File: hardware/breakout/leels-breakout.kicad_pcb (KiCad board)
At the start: 2 copper layers, 0 parts

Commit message: Breakout PCB: placement, routing and DRC-clean board
- build_pcb.py builds the board from the schematic netlist: outline (stops
  at the DevKit's PCB edge, nothing under the antenna), placement with
  the buffer and passives under the DevKit, terminals facing the edges,
  GND pours on both layers and stitching vias.
- route.py round-trips through Freerouting (Specctra DSN/SES); GND is
  left to the pours.
- leels.pretty: Espressif's DevKitC-1 footprint with the courtyard
  limited to the socket rows.
- Q1 on TO-92_Inline_Wide (the narrow one breaks 0.25 mm clearance).
- Net classes: 0.3 mm signals, 0.6 mm power and ground.
DRC: 0 violations, 0 unconnected, 0 schematic parity issues.

Co-Authored-By: Claude Opus 5.5 <noreply@anthropic.com>
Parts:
- added C1: 100n, Capacitor_THT:C_Disc_D5.0mm_W2.5mm_P5.00mm, F.Cu at (19.5, 45.2)
- added C2: 10u 16V, Capacitor_THT:CP_Radial_D5.0mm_P2.00mm, F.Cu at (29.5, 45.9)
- added D1: 1N5817, Diode_THT:D_DO-41_SOD81_P10.16mm_Horizontal, F.Cu at (25.0, 69.0)
- added J2: Servo, TerminalBlock_Phoenix:TerminalBlock_Phoenix_MKDS-1,5-5-5.08_1x05_P5.08mm_Horizontal, F.Cu at (45.5, 35.0)
- added J3: Encoder, TerminalBlock_Phoenix:TerminalBlock_Phoenix_MKDS-1,5-5-5.08_1x05_P5.08mm_Horizontal, F.Cu at (5.50, 43.0)
- added J4: 5V in, TerminalBlock_Phoenix:TerminalBlock_Phoenix_MKDS-1,5-2-5.08_1x02_P5.08mm_Horizontal, F.Cu at (45.5, 62.0)
- added J5: Nextion, Connector_JST:JST_XH_B4B-XH-A_1x04_P2.50mm_Vertical, F.Cu at (46.0, 27.7)
- added J6: Shield GND, TerminalBlock_Phoenix:TerminalBlock_Phoenix_MKDS-1,5-3-5.08_1x03_P5.08mm_Horizontal, F.Cu at (5.50, 61.2)
- added Q1: 2N3904, Package_TO_SOT_THT:TO-92_Inline_Wide, F.Cu at (24.1, 13.0)
- added R1: 1k, Resistor_THT:R_Axial_DIN0207_L6.3mm_D2.5mm_P7.62mm_Horizontal, F.Cu at (33.0, 17.0)
- added R2: 10k, Resistor_THT:R_Axial_DIN0207_L6.3mm_D2.5mm_P7.62mm_Horizontal, F.Cu at (25.4, 20.5)
- added R3: 4k7, Resistor_THT:R_Axial_DIN0207_L6.3mm_D2.5mm_P7.62mm_Horizontal, F.Cu at (16.8, 52.0)
- added R4: 4k7, Resistor_THT:R_Axial_DIN0207_L6.3mm_D2.5mm_P7.62mm_Horizontal, F.Cu at (16.8, 55.5)
- added R5: 10k, Resistor_THT:R_Axial_DIN0207_L6.3mm_D2.5mm_P7.62mm_Horizontal, F.Cu at (27.0, 52.0)
- added R6: 10k, Resistor_THT:R_Axial_DIN0207_L6.3mm_D2.5mm_P7.62mm_Horizontal, F.Cu at (27.0, 55.5)
- added R7: 4k7, Resistor_THT:R_Axial_DIN0207_L6.3mm_D2.5mm_P7.62mm_Horizontal, F.Cu at (16.8, 59.0)
- added U1: ESP32-C6-DevKitC-1, leels:ESP32-C6-DevKitC-1_Sockets, F.Cu at (14.0, 10.0)
- added U2: 74AHCT125, Package_DIP:DIP-14_W7.62mm, F.Cu at (32.0, 40.5)
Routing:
- net +5V: track 0.00 -> 96.5 mm
- net ENC_Z: track 0.00 -> 73.7 mm
- net +3V3: track 0.00 -> 72.4 mm
- net Net-(J2-Pin_4): track 0.00 -> 44.6 mm
- net Net-(J3-Pin_4): track 0.00 -> 38.0 mm
- net Net-(U1-GPIO19): track 0.00 -> 33.0 mm
- net Net-(J3-Pin_3): track 0.00 -> 32.7 mm
- net Net-(J2-Pin_3): track 0.00 -> 26.4 mm
- net Net-(U1-GPIO18): track 0.00 -> 24.0 mm
- net Net-(J2-Pin_2): track 0.00 -> 15.4 mm
- net Net-(D1-A): track 0.00 -> 13.2 mm
- net Net-(U1-GPIO20): track 0.00 -> 13.1 mm
- net Net-(J5-Pin_3): track 0.00 -> 9.16 mm
- net Net-(J5-Pin_4): track 0.00 -> 9.14 mm
- net Net-(Q1-B): track 0.00 -> 8.02 mm
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- added copper zone on B.Cu, net GND
- added copper zone on F.Cu, net GND
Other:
- board outline added: 51 x 63.6 mm
- rule pad_to_mask_clearance: 0.05 -> 0

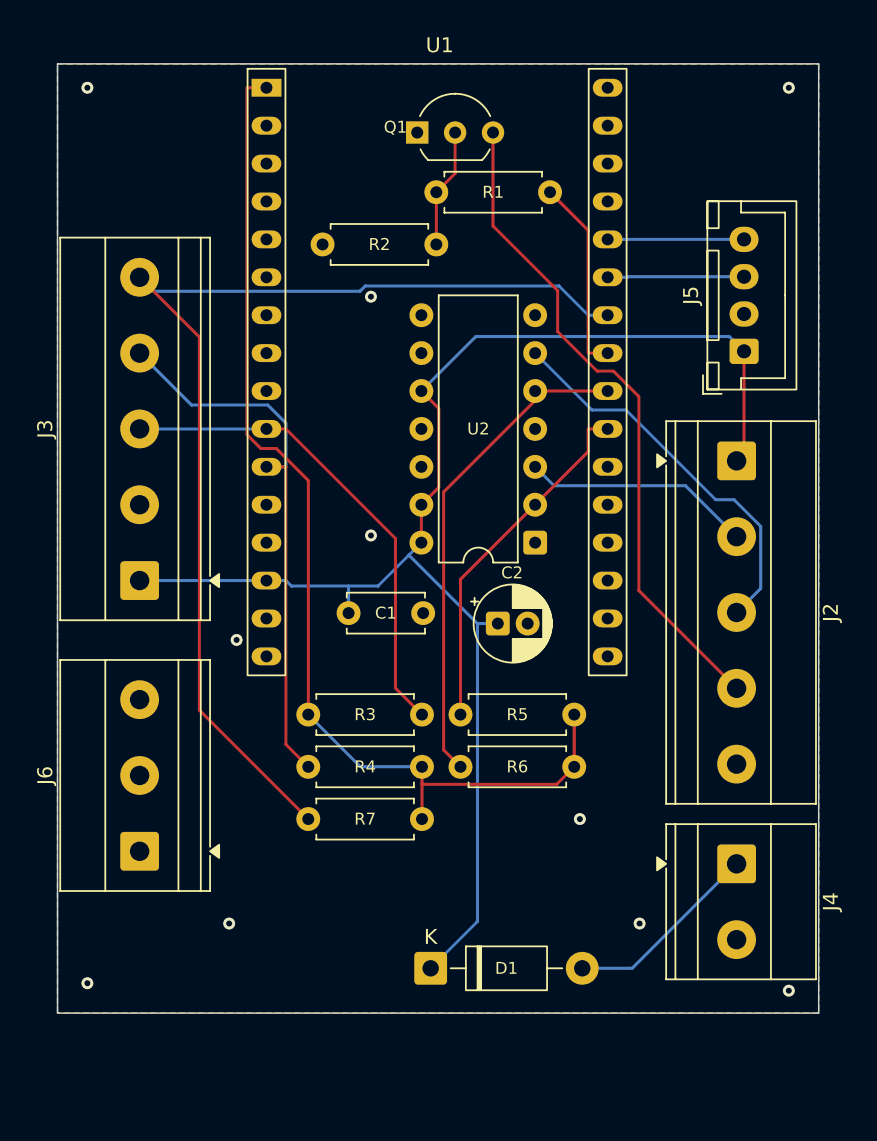
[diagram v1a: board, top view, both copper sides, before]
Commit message: Breakout PCB: caps out from under the DevKit, connector silkscreen
- C1/C2 move below the DevKit (too tall for the ~7 mm under it), next to
  the 5 V input.
- Pin labels beside every terminal and the Nextion header (the display's
  pin names), group titles, board name and orientation on the back.
- Re-routed; DRC 0 violations, 0 unconnected, 0 parity issues.

Co-Authored-By: Claude Opus 5.5 <noreply@anthropic.com>
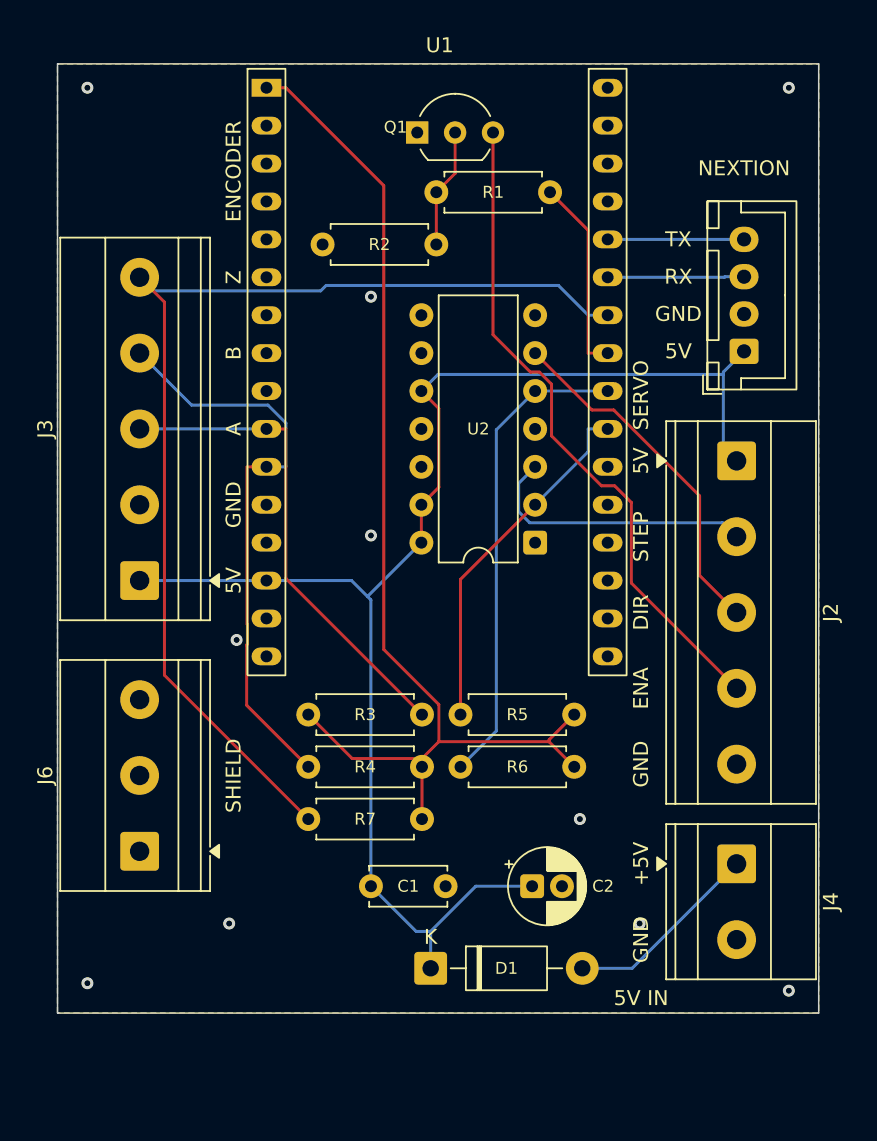
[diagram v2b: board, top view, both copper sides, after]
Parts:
- moved C1 18.4 mm to (21.0, 63.5)
- moved C2 17.7 mm to (31.8, 63.5)
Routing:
- net +3V3: track 72.4 -> 76.1 mm
- net Net-(J2-Pin_2): track 15.4 -> 18.8 mm
- net Net-(J2-Pin_3): track 26.4 -> 23.8 mm
- net Net-(J3-Pin_4): track 38.0 -> 39.1 mm
- net Net-(U1-GPIO19): track 33.0 -> 32.1 mm
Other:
- board text added: "+5V"
- board text added: "5V"
- board text added: "5V IN"
- board text added: "A"
- board text added: "B"
- board text added: "DIR"
- board text added: "DevKitC-1 on top, USB down"
- board text added: "ENA"
- board text added: "ENCODER"
- board text added: "GND"
- board text added: "NEXTION"
- board text added: "RX"
- board text added: "SERVO"
- board text added: "SHIELD"
- board text added: "STEP"
- board text added: "TX"
- board text added: "Z"
- board text added: "leels breakout rev A"

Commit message: Breakout PCB review fixes: terminals face out, real track widths
- Every screw terminal opened towards the DevKit (checked in a 3D
  render); turned all four 180 degrees so wires enter from the edges.
- The routed board was 0.2 mm everywhere: standalone pcbnew doesn't put
  the project's net classes into the DSN. route.py now writes the DSN net
  classes itself: 0.6 mm power, 0.3 mm signals, 0.25 mm clearance.
- Connector references to F.Fab (titles name them), two more stitching
  vias, 3D render added.
DRC: 1 warning (J5 GND thermal on B.Cu, connected via F.Cu), 0
unconnected, 0 parity issues.

Co-Authored-By: Claude Opus 5.5 <noreply@anthropic.com>
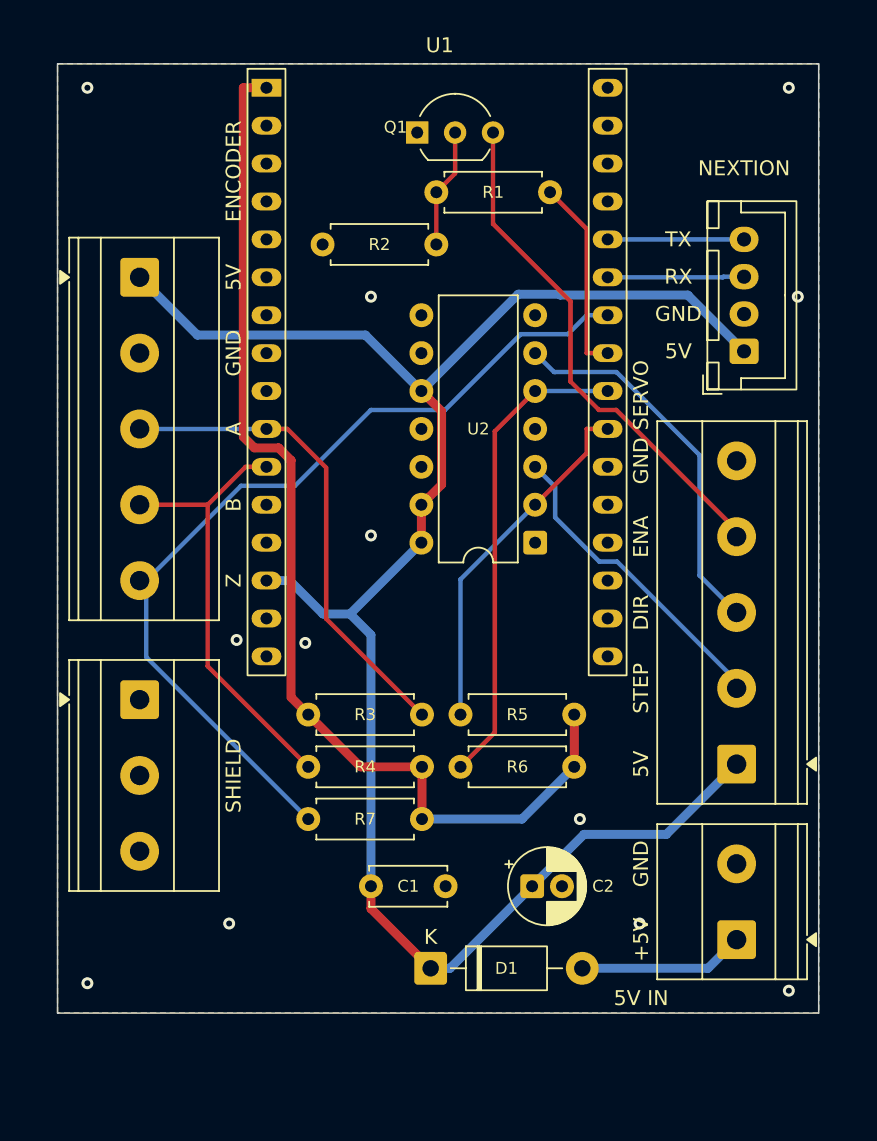
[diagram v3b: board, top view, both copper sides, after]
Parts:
- moved J3 20.3 mm to (5.50, 22.7), turned to -90 degrees
- moved J2 20.3 mm to (45.5, 55.3), turned to 90 degrees
- moved J6 10.2 mm to (5.50, 51.0), turned to -90 degrees
- moved J4 5.08 mm to (45.5, 67.1), turned to 90 degrees
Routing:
- net +5V: track 96.2 -> 124.6 mm
- net ENC_Z: track 73.7 -> 59.2 mm
- net Net-(J2-Pin_4): track 44.9 -> 34.5 mm
- net Net-(J3-Pin_4): track 39.1 -> 29.9 mm
- net Net-(J2-Pin_2): track 18.8 -> 21.1 mm
- net +3V3: track 76.1 -> 74.0 mm
- net Net-(D1-A): track 13.2 -> 11.1 mm
- net Net-(J2-Pin_3): track 23.8 -> 25.4 mm
- net GND: vias 10 -> 12

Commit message: Breakout rev A: encoder RC filters, Nextion before D1, Dupont header, holes
- Encoder A/B/Z: 220R series at the terminal, 220p to GND at the GPIO
  (with the existing 4k7 pull-up), for noise and ESD.
- Nextion power (J5, new J7) on 5V_IN ahead of D1: no Schottky drop for
  the display; it needs J4 power.
- J7: 1x4 2.54 mm header in parallel with the JST for Dupont plugs.
- C1 axial (laid flat) right at U2's supply pin; Q1 laid flat
  (TO-92 staggered horizontal, clearance-safe).
- Three M3 mounting holes; board 51 x 70.1 mm.
DRC: 1 warning (U2 pin 12 thermal on F.Cu, connected via B.Cu), 0
unconnected, 0 parity issues; ERC clean.

Co-Authored-By: Claude Opus 5.5 <noreply@anthropic.com>
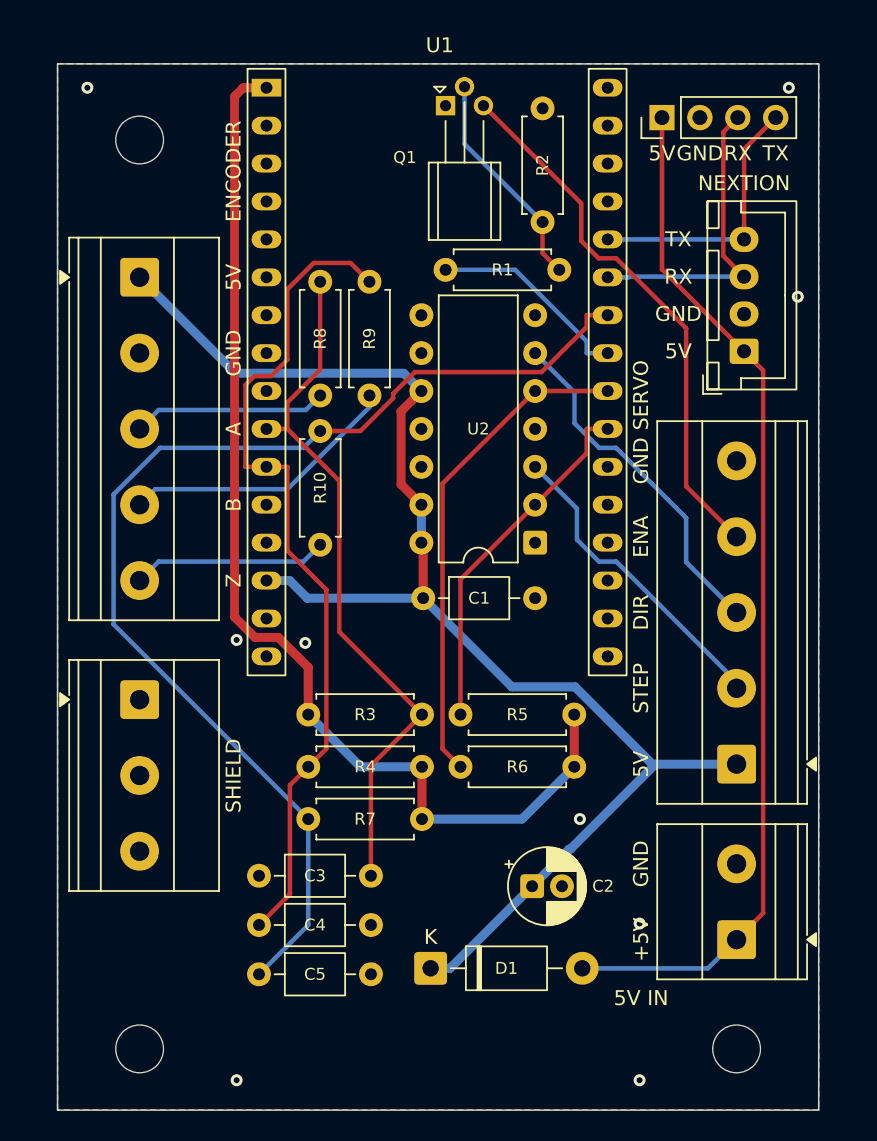
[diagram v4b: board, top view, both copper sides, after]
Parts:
- added C3: 220p, Capacitor_THT:C_Axial_L3.8mm_D2.6mm_P7.50mm_Horizontal, F.Cu at (13.5, 62.8)
- added C4: 220p, Capacitor_THT:C_Axial_L3.8mm_D2.6mm_P7.50mm_Horizontal, F.Cu at (13.5, 66.1)
- added C5: 220p, Capacitor_THT:C_Axial_L3.8mm_D2.6mm_P7.50mm_Horizontal, F.Cu at (13.5, 69.4)
- added H1: MountingHole_3.2mm_M3, MountingHole:MountingHole_3.2mm_M3, F.Cu at (5.50, 13.5)
- added H2: MountingHole_3.2mm_M3, MountingHole:MountingHole_3.2mm_M3, F.Cu at (5.50, 74.4)
- added H3: MountingHole_3.2mm_M3, MountingHole:MountingHole_3.2mm_M3, F.Cu at (45.5, 74.4)
- added J7: Nextion (Dupont), Connector_PinHeader_2.54mm:PinHeader_1x04_P2.54mm_Vertical, F.Cu at (40.5, 12.0)
- added R10: 220, Resistor_THT:R_Axial_DIN0207_L6.3mm_D2.5mm_P7.62mm_Horizontal, F.Cu at (17.6, 40.6)
- added R8: 220, Resistor_THT:R_Axial_DIN0207_L6.3mm_D2.5mm_P7.62mm_Horizontal, F.Cu at (17.6, 30.6)
- added R9: 220, Resistor_THT:R_Axial_DIN0207_L6.3mm_D2.5mm_P7.62mm_Horizontal, F.Cu at (20.9, 30.6)
- C1: footprint Capacitor_THT:C_Disc_D5.0mm_W2.5mm_P5.00mm -> Capacitor_THT:C_Axial_L3.8mm_D2.6mm_P7.50mm_Horizontal
- Q1: footprint Package_TO_SOT_THT:TO-92_Inline_Wide -> Package_TO_SOT_THT:TO-92_W4.0mm_StaggerEven_Horizontal_FlatSideDown
- moved C1 19.6 mm to (24.5, 44.2)
- moved R1 8.72 mm to (26.0, 22.2), turned to 0 degrees
- moved R2 7.28 mm to (32.5, 19.0), turned to 90 degrees
- moved Q1 2.62 mm to (26.0, 11.2)
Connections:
- net Net-(J5-Pin_3) renamed NX_TX
- net Net-(J5-Pin_4) renamed NX_RX
- D1 pad 2: Net-(D1-A) -> 5V_IN
- J3 pad 5: ENC_Z -> Net-(J3-Pin_5)
- J4 pad 1: Net-(D1-A) -> 5V_IN
- J5 pad 1: +5V -> 5V_IN
- R3 pad 2: Net-(J3-Pin_3) -> Net-(U1-GPIO10)
- R4 pad 1: Net-(J3-Pin_4) -> Net-(U1-GPIO11)
- U1 pad 10: Net-(J3-Pin_3) -> Net-(U1-GPIO10)
- U1 pad 11: Net-(J3-Pin_4) -> Net-(U1-GPIO11)
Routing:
- net 5V_IN: track 0.00 -> 69.8 mm
- net Net-(U1-GPIO11): track 0.00 -> 56.9 mm
- net Net-(U1-GPIO10): track 0.00 -> 47.3 mm
- net +5V: track 124.6 -> 94.4 mm
- net Net-(J3-Pin_3): track 32.8 -> 13.0 mm
- net ENC_Z: track 59.2 -> 77.6 mm
- net Net-(J3-Pin_5): track 0.00 -> 13.1 mm
- net NX_TX: track 9.16 -> 20.8 mm
- net Net-(D1-A): track 11.1 -> 0.00 mm
- net Net-(J3-Pin_4): track 29.9 -> 18.9 mm
- net NX_RX: track 9.14 -> 18.2 mm
- net Net-(Q1-B): track 8.02 -> 14.9 mm
- net Net-(J2-Pin_4): track 34.5 -> 36.6 mm
- net Net-(J2-Pin_3): track 25.4 -> 23.6 mm
- net Net-(U1-GPIO19): track 32.1 -> 33.1 mm
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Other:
- board size 51 x 63.6 mm -> 51 x 70.1 mm

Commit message: Breakout: 1.0 mm holes / 1.7 mm pads for the DevKit sockets
Standard female headers (as in KiCad's PinSocket footprints) need 1.0 mm
holes; Espressif's footprint had 0.8 mm. Re-routed; DRC 1 warning (U1
pin 15 thermal on F.Cu, connected via B.Cu), 0 unconnected, 0 parity.

Co-Authored-By: Claude Opus 5.5 <noreply@anthropic.com>
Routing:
- net ENC_Z: track 77.6 -> 62.1 mm
- net Net-(U1-GPIO10): track 47.3 -> 59.7 mm
- net Net-(U1-GPIO11): track 56.9 -> 50.6 mm, vias 0 -> 1
- net +5V: track 94.4 -> 99.0 mm
- net +3V3: track 74.5 -> 70.9 mm
- net Net-(J3-Pin_3): track 13.0 -> 14.3 mm
- net Net-(U1-GPIO19): track 33.1 -> 32.1 mm
